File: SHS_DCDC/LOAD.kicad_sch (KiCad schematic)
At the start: 33 parts, among them Q2 PMV100XPEAR, Q3 2N7002, Q4 2N7002, Q5 PMV100XPEAR, Q6 2N7002, Q7 PMV100XPEAR

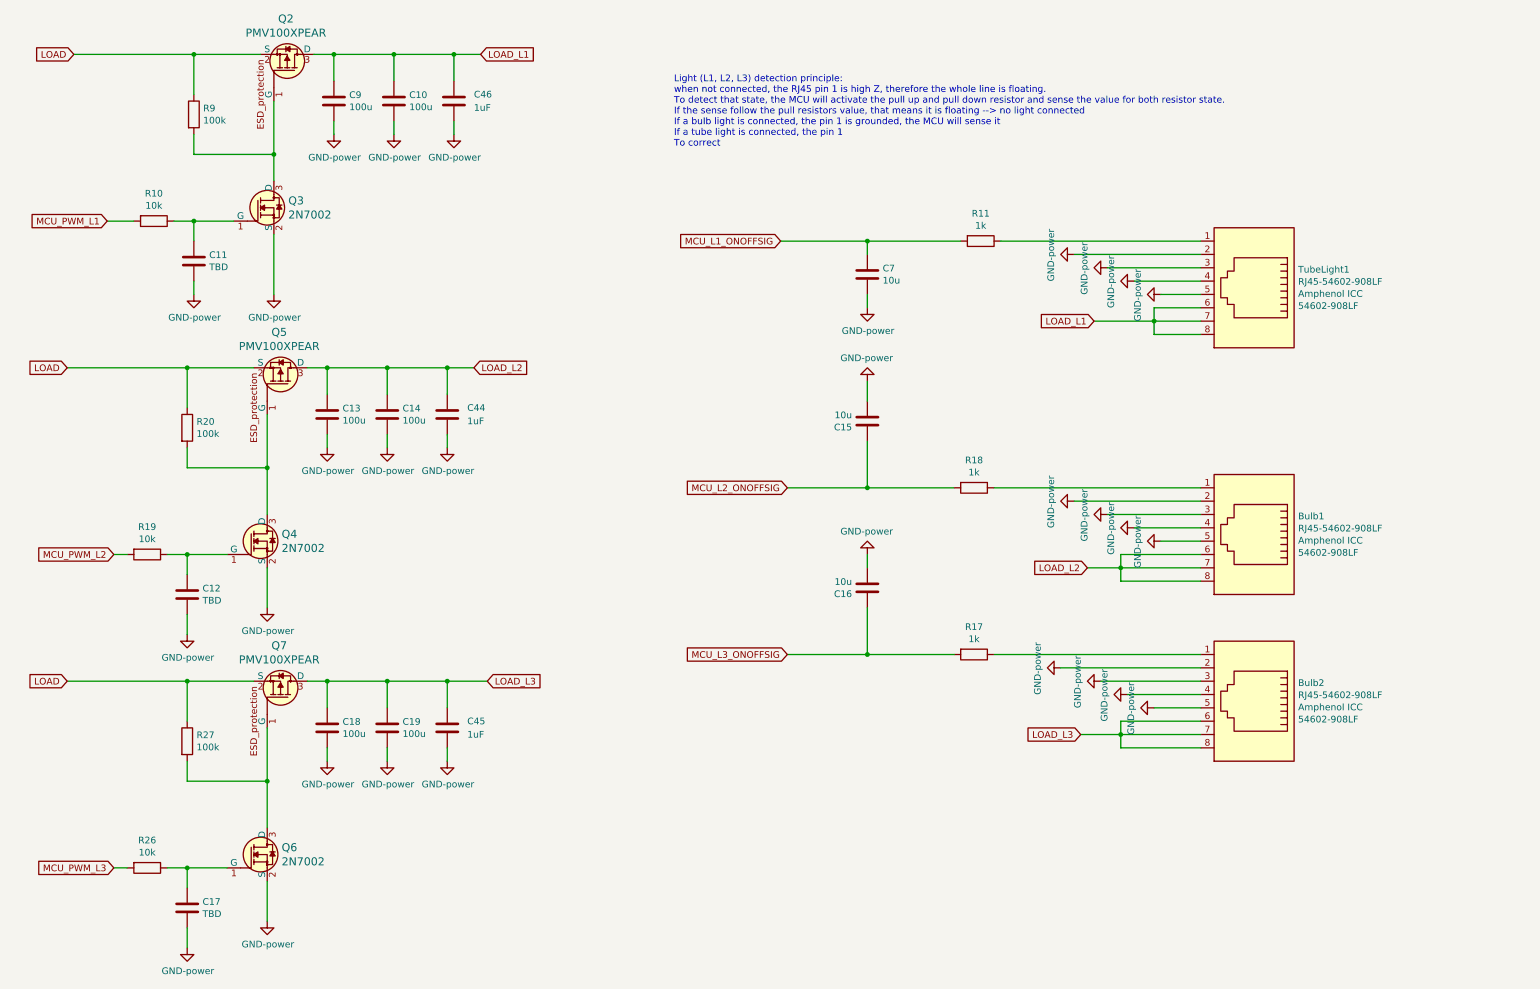
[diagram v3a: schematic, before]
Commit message: Light bulb drive update
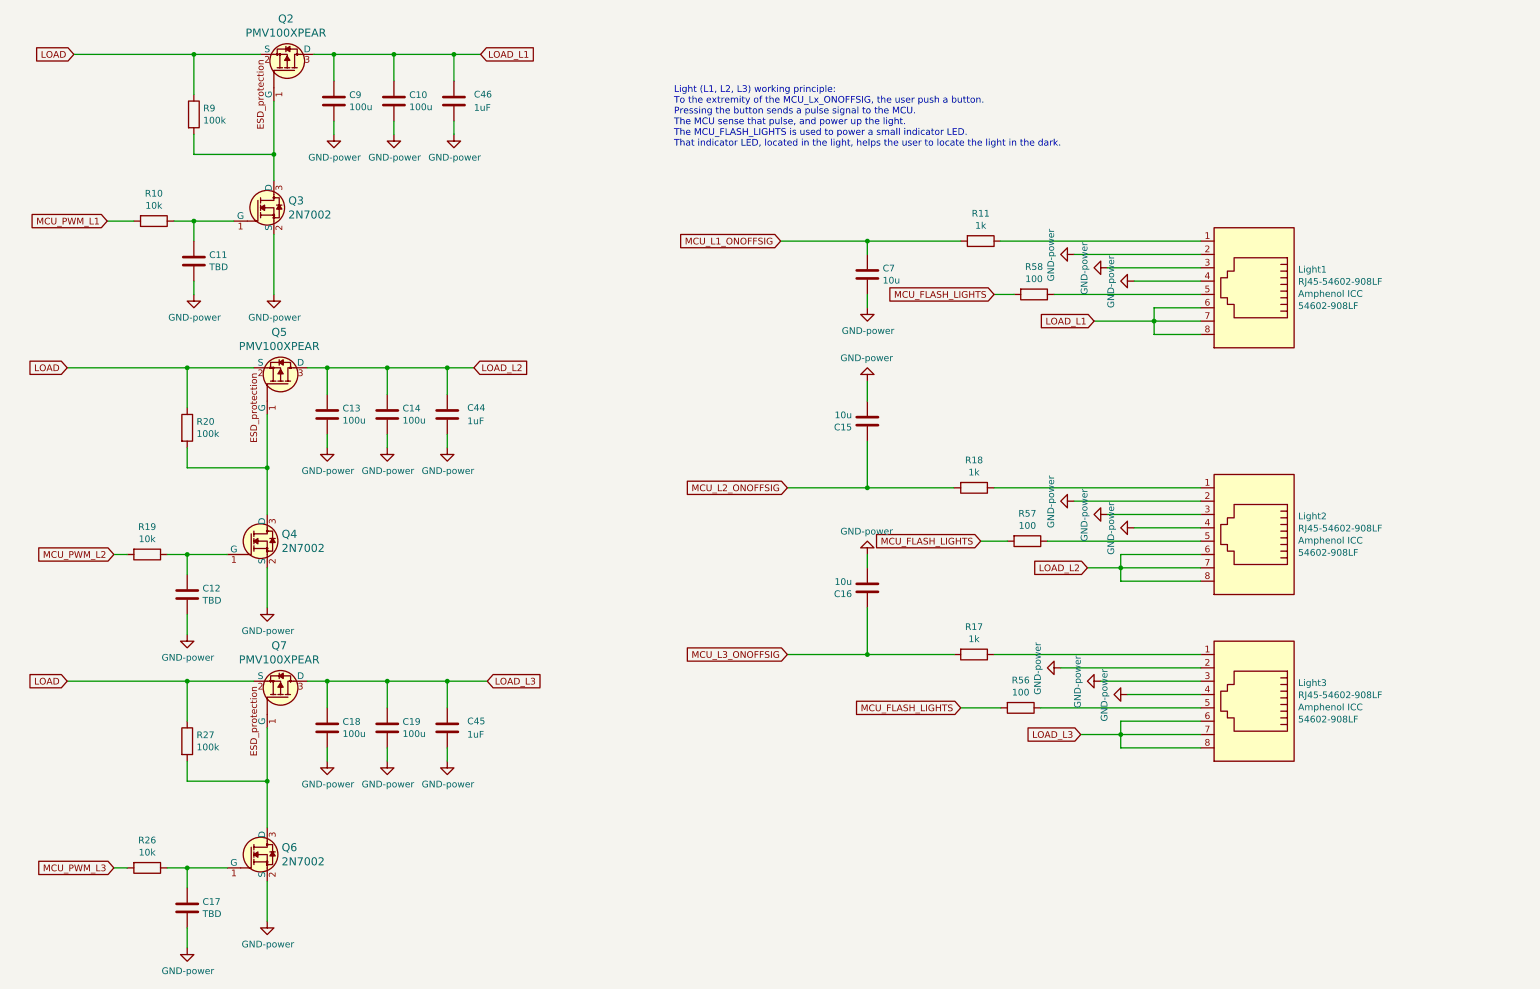
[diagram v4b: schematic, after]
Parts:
- added R56, R57, R58: 100, Resistor_SMD:R_0603_1608Metric, symbol SHS_DCDC:R-Device
- renumbered TubeLight1 to Light1, Bulb1 to Light2, Bulb2 to Light3
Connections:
- net GND: no longer Light1.5, Light2.5, Light3.5
- new net: Light1.5, R58.1
- new net: Light2.5, R57.1
- new net: Light3.5, R56.1
- new net MCU_FLASH_LIGHTS: R56.2, R57.2, R58.2
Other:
- note added: "Light (L1, L2, L3) working principle: To the extremity of the MCU_Lx_ONOFFSIG, the user push a button. Pressing the button sends a pulse signal to the MCU. The MCU sense that pulse, and power up the light. The MCU_FLASH_LIGHTS is used to power a small indicator LED. That indicator LED, located in the light, helps the user to locate the light in the dark."
- note removed: "Light (L1, L2, L3) detection principle: when not connected, the RJ45 pin 1 is high Z, therefore the whole line is floating. To detect that state, the MCU will activate the pull up and pull down resistor and sense the value for both resistor state. If the sense follow the pull resistors value, that means it is floating --> no light connected If a bulb light is connected, the pin 1 is grounded, the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"
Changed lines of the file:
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@@
+    (stroke (width 0) (type default) (color 0 0 0 0))
+  )
+  (wire (pts (xy 195.58 114.3) (xy 200.66 114.3))
     (stroke (width 0) (type default) (color 0 0 0 0))
   )
@@
     (stroke (width 0) (type default) (color 0 0 0 0))
   )
+  (wire (pts (xy 191.77 146.05) (xy 199.39 146.05))
+    (stroke (width 0) (type default) (color 0 0 0 0))
+  )
   (wire (pts (xy 237.49 153.67) (xy 222.25 153.67))
     (stroke (width 0) (type default) (color 0 0 0 0))
@@
     (stroke (width 0) (type default) (color 0 0 0 0))
   )
+  (wire (pts (xy 198.12 67.31) (xy 201.93 67.31))
+    (stroke (width 0) (type default) (color 0 0 0 0))
+  )
   (wire (pts (xy 93.98 81.28) (xy 99.06 81.28))
     (stroke (width 0) (type default) (color 0 0 0 0))
@@
     (stroke (width 0) (type default) (color 0 0 0 0))
   )
-  (wire (pts (xy 237.49 67.31) (xy 229.87 67.31))
+  (wire (pts (xy 209.55 67.31) (xy 237.49 67.31))
     (stroke (width 0) (type default) (color 0 0 0 0))
   )
@@
     (stroke (width 0) (type default) (color 0 0 0 0))
   )
-  (wire (pts (xy 237.49 146.05) (xy 228.6 146.05))
-    (stroke (width 0) (type default) (color 0 0 0 0))
-  )
   (wire (pts (xy 210.82 138.43) (xy 237.49 138.43))
     (stroke (width 0) (type default) (color 0 0 0 0))
@@
     (stroke (width 0) (type default) (color 0 0 0 0))
   )
-  (wire (pts (xy 237.49 114.3) (xy 229.87 114.3))
+  (wire (pts (xy 208.28 114.3) (xy 237.49 114.3))
     (stroke (width 0) (type default) (color 0 0 0 0))
   )
@@
     (stroke (width 0) (type default) (color 0 0 0 0))
   )
+  (wire (pts (xy 207.01 146.05) (xy 237.49 146.05))
+    (stroke (width 0) (type default) (color 0 0 0 0))
+  )
   (wire (pts (xy 215.9 119.38) (xy 222.25 119.38))
     (stroke (width 0) (type default) (color 0 0 0 0))
@@
     (stroke (width 0) (type default) (color 0 0 0 0))
   )
-  (text "Light (L1, L2, L3) detection principle:\nwhen not connected, the RJ45 pin 1 is high Z, therefore the whole line is floating.\nTo detect that state, the MCU will activate the pull up and pull down resistor and sense the value for both resistor state.\nIf the sense follow the pull resistors value, that means it is floating --> no light connected\nIf a bulb light is connected, the pin 1 is grounded, the MCU will sense it\nIf a tube light is connected, the pin 1 \nTo correct"
+  (text "Light (L1, L2, L3) working principle:\nTo the extremity of the MCU_Lx_ONOFFSIG, the user push a button.\nPressing the button sends a pulse signal to the MCU.\nThe MCU sense that pulse, and power up the light.\nThe MCU_FLASH_LIGHTS is used to power a small indicator LED.\nThat indicator LED, located in the light, helps the user to locate the light in the dark."
     (at 137.16 39.37 0)
     (effects (font (size 1.27 1.27)) (justify left bottom))
@@
     )
   )
+  (global_label "MCU_FLASH_LIGHTS" (shape input) (at 195.58 114.3 180) (fields_autoplaced)
+    (effects (font (size 1.27 1.27)) (justify right))
+    (property "Intersheet References" "${INTERSHEET_REFS}" (id 0) (at 175.1129 114.2206 0)
+      (effects (font (size 1.27 1.27)) (justify right) hide)
+    )
+  )
+  (global_label "MCU_FLASH_LIGHTS" (shape input) (at 191.77 146.05 180) (fields_autoplaced)
+    (effects (font (size 1.27 1.27)) (justify right))
+    (property "Intersheet References" "${INTERSHEET_REFS}" (id 0) (at 171.3029 145.9706 0)
+      (effects (font (size 1.27 1.27)) (justify right) hide)
+    )
+  )
   (global_label "MCU_PWM_L2" (shape input) (at 30.48 116.84 180) (fields_autoplaced)
     (effects (font (size 1.27 1.27)) (justify right))
@@
     )
   )
+  (global_label "MCU_FLASH_LIGHTS" (shape input) (at 198.12 67.31 180) (fields_autoplaced)
+    (effects (font (size 1.27 1.27)) (justify right))
+    (property "Intersheet References" "${INTERSHEET_REFS}" (id 0) (at 177.6529 67.2306 0)
+      (effects (font (size 1.27 1.27)) (justify right) hide)
+    )
+  )
   (global_label "MCU_PWM_L3" (shape input) (at 30.48 176.53 180) (fields_autoplaced)
     (effects (font (size 1.27 1.27)) (justify right))
@@
   (symbol (lib_id "SHS_DCDC:RJ45-54602-908LF") (at 247.65 64.77 180) (unit 1)
     (in_bom yes) (on_board yes)
-    (property "Reference" "TubeLight1" (id 0) (at 256.032 62.5602 0)
+    (property "Reference" "Light1" (id 0) (at 256.032 62.5602 0)
       (effects (font (size 1.27 1.27)) (justify right))
     )
@@
   (symbol (lib_id "SHS_DCDC:RJ45-54602-908LF") (at 247.65 111.76 180) (unit 1)
     (in_bom yes) (on_board yes)
-    (property "Reference" "Bulb1" (id 0) (at 256.032 109.5502 0)
+    (property "Reference" "Light2" (id 0) (at 256.032 109.5502 0)
       (effects (font (size 1.27 1.27)) (justify right))
     )
@@
   (symbol (lib_id "SHS_DCDC:RJ45-54602-908LF") (at 247.65 143.51 180) (unit 1)
     (in_bom yes) (on_board yes)
-    (property "Reference" "Bulb2" (id 0) (at 256.032 141.3002 0)
+    (property "Reference" "Light3" (id 0) (at 256.032 141.3002 0)
       (effects (font (size 1.27 1.27)) (justify right))
     )
@@
     (pin "2")
   )
-  (symbol (lib_id "SHS_DCDC:GND-power") (at 229.87 114.3 270) (unit 1)
-    (in_bom yes) (on_board yes)
-    (property "Reference" "#PWR020" (id 0) (at 223.52 114.3 0)
-      (effects (font (size 1.27 1.27)) hide)
-    )
-    (property "Value" "GND-power" (id 1) (at 225.4758 114.427 0))
-    (property "Footprint" "" (id 2) (at 229.87 114.3 0)
-      (effects (font (size 1.27 1.27)) hide)
-    )
-    (property "Datasheet" "" (id 3) (at 229.87 114.3 0)
-      (effects (font (size 1.27 1.27)) hide)
-    )
-    (pin "1")
-  )
-  (symbol (lib_id "SHS_DCDC:GND-power") (at 229.87 67.31 270) (unit 1)
-    (in_bom yes) (on_board yes)
-    (property "Reference" "#PWR09" (id 0) (at 223.52 67.31 0)
-      (effects (font (size 1.27 1.27)) hide)
-    )
-    (property "Value" "GND-power" (id 1) (at 225.4758 67.437 0))
-    (property "Footprint" "" (id 2) (at 229.87 67.31 0)
-      (effects (font (size 1.27 1.27)) hide)
-    )
-    (property "Datasheet" "" (id 3) (at 229.87 67.31 0)
-      (effects (font (size 1.27 1.27)) hide)
-    )
-    (pin "1")
-  )
   (symbol (lib_id "SHS_DCDC:R-Device") (at 194.31 135.89 270) (unit 1)
     (in_bom yes) (on_board yes)
@@
     (pin "1")
   )
-  (symbol (lib_id "SHS_DCDC:GND-power") (at 228.6 146.05 270) (unit 1)
-    (in_bom yes) (on_board yes)
-    (property "Reference" "#PWR028" (id 0) (at 222.25 146.05 0)
-      (effects (font (size 1.27 1.27)) hide)
-    )
-    (property "Value" "GND-power" (id 1) (at 224.2058 146.177 0))
-    (property "Footprint" "" (id 2) (at 228.6 146.05 0)
-      (effects (font (size 1.27 1.27)) hide)
-    )
-    (property "Datasheet" "" (id 3) (at 228.6 146.05 0)
-      (effects (font (size 1.27 1.27)) hide)
-    )
-    (pin "1")
-  )
   (symbol (lib_id "SHS_DCDC:C-Device") (at 173.99 91.44 180) (unit 1)
     (in_bom yes) (on_board yes)
@@
       (effects (font (size 1.27 1.27)) hide)
     )
+    (pin "1")
+    (pin "2")
+  )
+  (symbol (lib_id "SHS_DCDC:R-Device") (at 204.47 114.3 270) (unit 1)
+    (in_bom yes) (on_board yes)
+    (property "Reference" "R57" (id 0) (at 204.47 109.0422 90))
+    (property "Value" "100" (id 1) (at 204.47 111.3536 90))
+    (property "Footprint" "Resistor_SMD:R_0603_1608Metric" (id 2) (at 204.47 112.522 90)
+      (effects (font (size 1.27 1.27)) hide)
+    )
+    (property "Datasheet" "~" (id 3) (at 204.47 114.3 0)
+      (effects (font (size 1.27 1.27)) hide)
+    )
+    (pin "1")
+    (pin "2")
+  )
+  (symbol (lib_id "SHS_DCDC:R-Device") (at 203.2 146.05 270) (unit 1)
+    (in_bom yes) (on_board yes)
+    (property "Reference" "R56" (id 0) (at 203.2 140.7922 90))
+    (property "Value" "100" (id 1) (at 203.2 143.1036 90))
+    (property "Footprint" "Resistor_SMD:R_0603_1608Metric" (id 2) (at 203.2 144.272 90)
+      (effects (font (size 1.27 1.27)) hide)
+    )
+    (property "Datasheet" "~" (id 3) (at 203.2 146.05 0)
+      (effects (font (size 1.27 1.27)) hide)
+    )
+    (pin "1")
+    (pin "2")
+  )
+  (symbol (lib_id "SHS_DCDC:R-Device") (at 205.74 67.31 270) (unit 1)
+    (in_bom yes) (on_board yes)
+    (property "Reference" "R58" (id 0) (at 205.74 62.0522 90))
+    (property "Value" "100" (id 1) (at 205.74 64.3636 90))
+    (property "Footprint" "Resistor_SMD:R_0603_1608Metric" (id 2) (at 205.74 65.532 90)
+      (effects (font (size 1.27 1.27)) hide)
+    )
+    (property "Datasheet" "~" (id 3) (at 205.74 67.31 0)
+      (effects (font (size 1.27 1.27)) hide)
+    )

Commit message: Final_check stage
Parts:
- R11, R17, R18: value 1k -> 100
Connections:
- net MCU_L1_ONOFFSIG: no longer C7.1
- net MCU_L2_ONOFFSIG: no longer C15.1
- net MCU_L3_ONOFFSIG: no longer C16.1
- net at Light1.1, R11.1: now also C7.1
- net at Light2.1, R18.1: now also C15.1
- net at Light3.1, R17.1: now also C16.1
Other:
- note added: "Light (L1, L2, L3) working principle: To the extremity of the MCU_Lx_ONOFFSIG, the user push a button. Pressing the button sends a pulse signal to the MCU. The MCU sense that pulse, and power up the light. The MCU_FLASH_LIGHTS is used to power a small indicator LED. That indicator LED, placed inside the light, helps the user to locate the light in the dark."
- note removed: "Light (L1, L2, L3) working principle: To the extremity of the MCU_Lx_ONOFFSIG, the user push a button. Pressing the button sends a pulse signal to the MCU. The MCU sense that pulse, and power up the light. The MCU_FLASH_LIGHTS is used to power a small indicator LED. That indicator LED, located in the light, helps the user to locate the light in the dark."
- moved on the sheet: C15, C16, R11, R17, R18
